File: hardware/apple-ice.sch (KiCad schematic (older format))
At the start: 5 parts

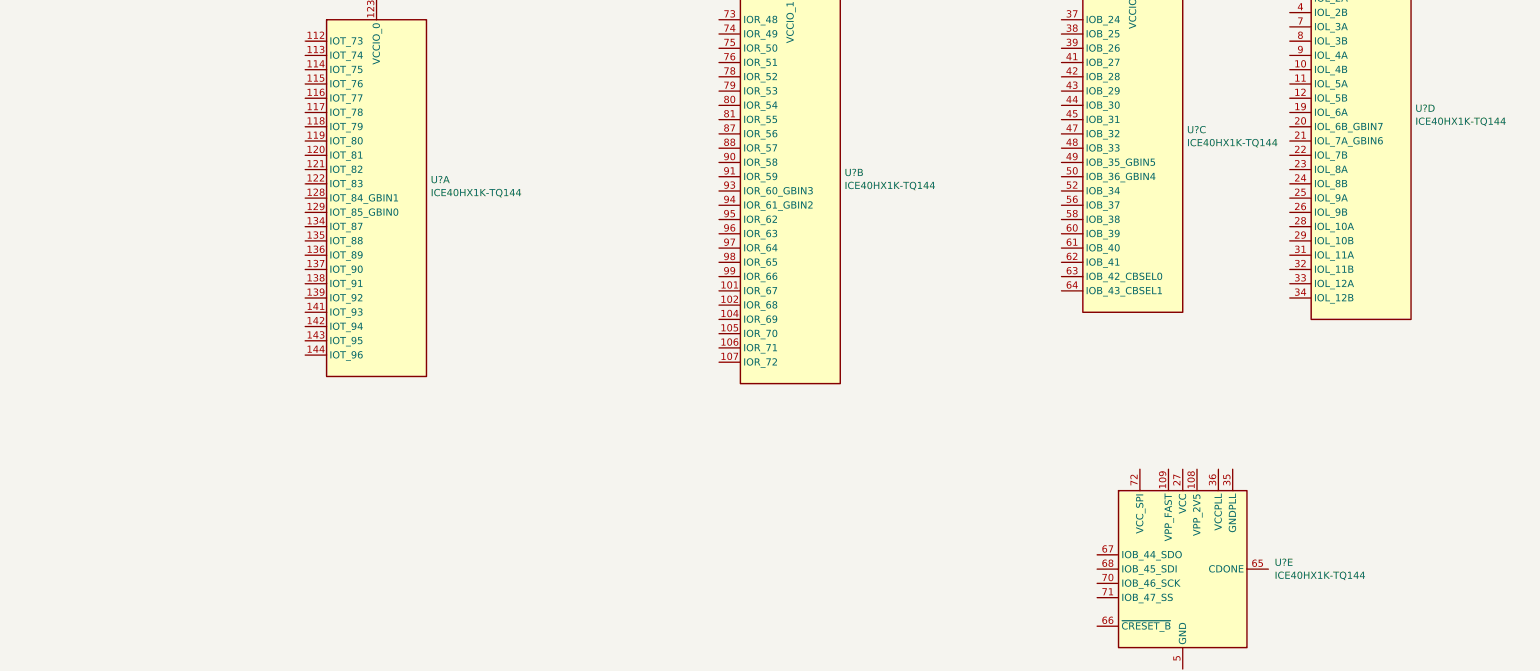
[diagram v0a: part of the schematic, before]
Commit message: Add apple 2 bus/cardedge symbol
Signed-off-by: Rangel Ivanov <rangelivanov88@gmail.com>
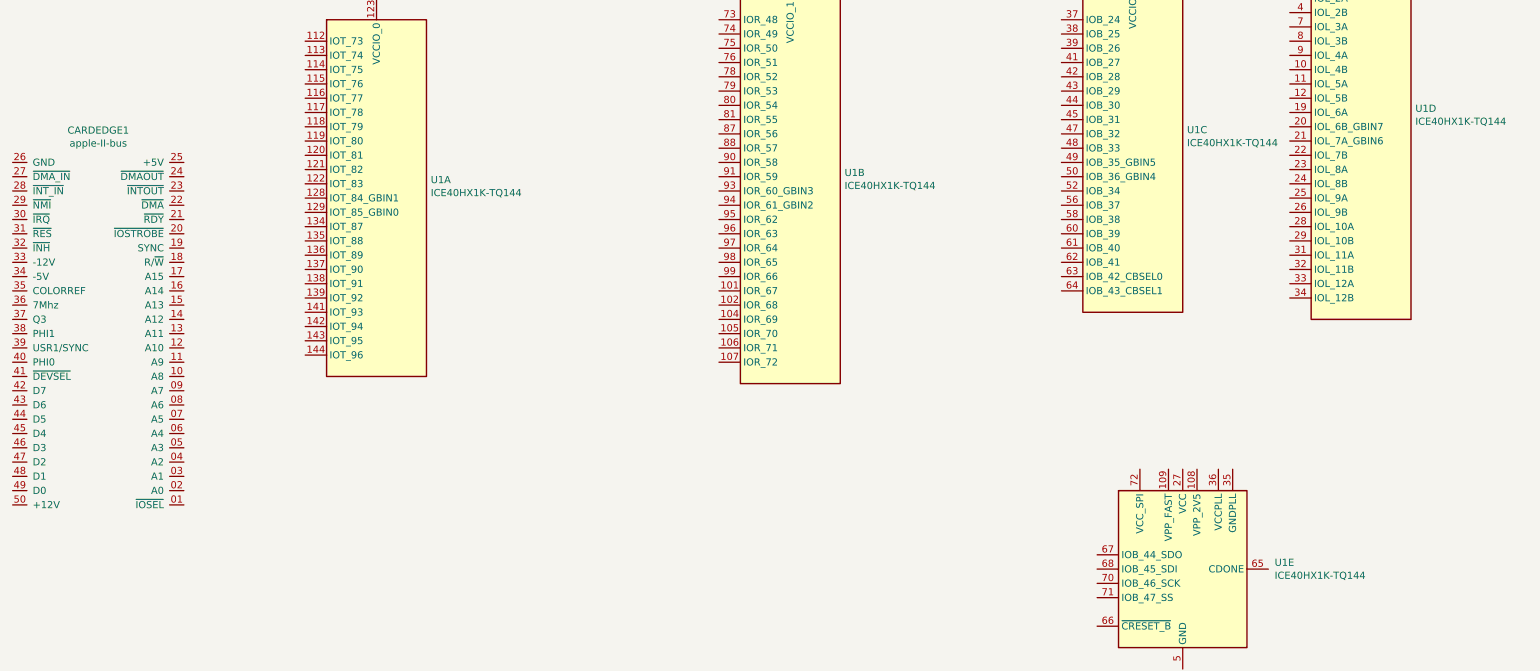
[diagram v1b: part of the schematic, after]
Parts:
- added CARDEDGE1: apple-II-bus, apple-ice:A2-50PIN-MINI, symbol apple-ice:apple-II-bus
- gave numbers to parts that had none: 1
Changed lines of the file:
@@
 $EndDescr
 $Comp
-L apple-ice:ICE40HX1K-TQ144 U?
+L apple-ice:ICE40HX1K-TQ144 U1
 U 1 1 609DDE92
 P 3500 2650
-F 0 "U?" H 3880 2778 50  0000 L CNN
+F 0 "U1" H 3880 2778 50  0000 L CNN
 F 1 "ICE40HX1K-TQ144" H 3880 2687 50  0000 L CNN
 F 2 "apple-ice:TQFP-144_20x20mm_P0.5mm" H 3500 1200 50  0001 C CNN
@@
 $EndComp
 $Comp
-L apple-ice:ICE40HX1K-TQ144 U?
+L apple-ice:ICE40HX1K-TQ144 U1
 U 2 1 609DFA1D
 P 6400 2600
-F 0 "U?" H 6780 2728 50  0000 L CNN
+F 0 "U1" H 6780 2728 50  0000 L CNN
 F 1 "ICE40HX1K-TQ144" H 6780 2637 50  0000 L CNN
 F 2 "apple-ice:TQFP-144_20x20mm_P0.5mm" H 6400 1150 50  0001 C CNN
@@
 $EndComp
 $Comp
-L apple-ice:ICE40HX1K-TQ144 U?
+L apple-ice:ICE40HX1K-TQ144 U1
 U 3 1 609E21D5
 P 8800 2300
-F 0 "U?" H 9180 2428 50  0000 L CNN
+F 0 "U1" H 9180 2428 50  0000 L CNN
 F 1 "ICE40HX1K-TQ144" H 9180 2337 50  0000 L CNN
 F 2 "apple-ice:TQFP-144_20x20mm_P0.5mm" H 8800 850 50  0001 C CNN
@@
 $EndComp
 $Comp
-L apple-ice:ICE40HX1K-TQ144 U?
+L apple-ice:ICE40HX1K-TQ144 U1
 U 4 1 609E4953
 P 10400 2150
-F 0 "U?" H 10780 2278 50  0000 L CNN
+F 0 "U1" H 10780 2278 50  0000 L CNN
 F 1 "ICE40HX1K-TQ144" H 10780 2187 50  0000 L CNN
 F 2 "apple-ice:TQFP-144_20x20mm_P0.5mm" H 10400 700 50  0001 C CNN
@@
 $EndComp
 $Comp
-L apple-ice:ICE40HX1K-TQ144 U?
+L apple-ice:ICE40HX1K-TQ144 U1
 U 5 1 609E76F0
 P 9150 5250
-F 0 "U?" H 9794 5296 50  0000 L CNN
+F 0 "U1" H 9794 5296 50  0000 L CNN
 F 1 "ICE40HX1K-TQ144" H 9794 5205 50  0000 L CNN
 F 2 "apple-ice:TQFP-144_20x20mm_P0.5mm" H 9150 3800 50  0001 C CNN
@@
 	1    0    0    -1
 $EndComp
+$Comp
+L apple-ice:apple-II-bus CARDEDGE1
+U 1 1 60F34519
+P 1550 2250
+F 0 "CARDEDGE1" H 1550 2325 50  0000 C CNN
+F 1 "apple-II-bus" H 1550 2234 50  0000 C CNN
+F 2 "apple-ice:A2-50PIN-MINI" H 1250 2200 50  0001 C CNN
+F 3 "" H 1250 2200 50  0001 C CNN
+	1    1550 2250
+	1    0    0    -1
+$EndComp

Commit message: Symbols and footprints
Signed-off-by: Rangel Ivanov <rangelivanov88@gmail.com>
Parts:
- added J?: USB_B_Micro, symbol apple-ice:USB_B_Micro
- added J?: Conn_02x05_Odd_Even, symbol apple-ice:Conn_02x05_Odd_Even
- added J? (x2): Conn_02x10_Odd_Even, symbol apple-ice:Conn_02x10_Odd_Even
- added U?: W25Q16JVSS, apple-ice:SOIC-8_5.23x5.23mm_P1.27mm, symbol apple-ice:W25Q16JVSS
- added U?: MCP1703A-1202_SOT223, apple-ice:SOT-223-3_TabPin2, symbol apple-ice:MCP1703A-1202_SOT223
- added U?: SN74LVC8T245PW, apple-ice:TSSOP-24_4.4x7.8mm_P0.65mm, symbol apple-ice:SN74LVC8T245PW
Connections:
- new net: U?.11 (GND), U?.12 (GND), U?.13 (GND)
- new net: U?.23 (VCC(B)), U?.24 (VCC(B))
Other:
- moved on the sheet: CARDEDGE1, U1A, U1B, U1C, U1D, U1E
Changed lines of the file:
@@
 L apple-ice:ICE40HX1K-TQ144 U1
 U 1 1 609DDE92
-P 3500 2650
-F 0 "U1" H 3880 2778 50  0000 L CNN
-F 1 "ICE40HX1K-TQ144" H 3880 2687 50  0000 L CNN
-F 2 "apple-ice:TQFP-144_20x20mm_P0.5mm" H 3500 1200 50  0001 C CNN
-F 3 "http://www.latticesemi.com/Products/FPGAandCPLD/iCE40" H 2650 4050 50  0001 C CNN
-	1    3500 2650
+P 3400 2150
+F 0 "U1" H 3780 2278 50  0000 L CNN
+F 1 "ICE40HX1K-TQ144" H 3780 2187 50  0000 L CNN
+F 2 "apple-ice:TQFP-144_20x20mm_P0.5mm" H 3400 700 50  0001 C CNN
+F 3 "http://www.latticesemi.com/Products/FPGAandCPLD/iCE40" H 2550 3550 50  0001 C CNN
+	1    3400 2150
 	1    0    0    -1
 $EndComp
@@
 L apple-ice:ICE40HX1K-TQ144 U1
 U 2 1 609DFA1D
-P 6400 2600
-F 0 "U1" H 6780 2728 50  0000 L CNN
-F 1 "ICE40HX1K-TQ144" H 6780 2637 50  0000 L CNN
-F 2 "apple-ice:TQFP-144_20x20mm_P0.5mm" H 6400 1150 50  0001 C CNN
-F 3 "http://www.latticesemi.com/Products/FPGAandCPLD/iCE40" H 5550 4000 50  0001 C CNN
-	2    6400 2600
+P 5350 2100
+F 0 "U1" H 5730 2228 50  0000 L CNN
+F 1 "ICE40HX1K-TQ144" H 5730 2137 50  0000 L CNN
+F 2 "apple-ice:TQFP-144_20x20mm_P0.5mm" H 5350 650 50  0001 C CNN
+F 3 "http://www.latticesemi.com/Products/FPGAandCPLD/iCE40" H 4500 3500 50  0001 C CNN
+	2    5350 2100
 	1    0    0    -1
 $EndComp
@@
 L apple-ice:ICE40HX1K-TQ144 U1
 U 3 1 609E21D5
-P 8800 2300
-F 0 "U1" H 9180 2428 50  0000 L CNN
-F 1 "ICE40HX1K-TQ144" H 9180 2337 50  0000 L CNN
-F 2 "apple-ice:TQFP-144_20x20mm_P0.5mm" H 8800 850 50  0001 C CNN
-F 3 "http://www.latticesemi.com/Products/FPGAandCPLD/iCE40" H 7950 3700 50  0001 C CNN
-	3    8800 2300
+P 7250 1900
+F 0 "U1" H 7630 2028 50  0000 L CNN
+F 1 "ICE40HX1K-TQ144" H 7630 1937 50  0000 L CNN
+F 2 "apple-ice:TQFP-144_20x20mm_P0.5mm" H 7250 450 50  0001 C CNN
+F 3 "http://www.latticesemi.com/Products/FPGAandCPLD/iCE40" H 6400 3300 50  0001 C CNN
+	3    7250 1900
 	1    0    0    -1
 $EndComp
@@
 L apple-ice:ICE40HX1K-TQ144 U1
 U 4 1 609E4953
-P 10400 2150
-F 0 "U1" H 10780 2278 50  0000 L CNN
-F 1 "ICE40HX1K-TQ144" H 10780 2187 50  0000 L CNN
-F 2 "apple-ice:TQFP-144_20x20mm_P0.5mm" H 10400 700 50  0001 C CNN
-F 3 "http://www.latticesemi.com/Products/FPGAandCPLD/iCE40" H 9550 3550 50  0001 C CNN
-	4    10400 2150
+P 9300 2000
+F 0 "U1" H 9680 2128 50  0000 L CNN
+F 1 "ICE40HX1K-TQ144" H 9680 2037 50  0000 L CNN
+F 2 "apple-ice:TQFP-144_20x20mm_P0.5mm" H 9300 550 50  0001 C CNN
+F 3 "http://www.latticesemi.com/Products/FPGAandCPLD/iCE40" H 8450 3400 50  0001 C CNN
+	4    9300 2000
 	1    0    0    -1
 $EndComp
@@
 L apple-ice:ICE40HX1K-TQ144 U1
 U 5 1 609E76F0
-P 9150 5250
-F 0 "U1" H 9794 5296 50  0000 L CNN
-F 1 "ICE40HX1K-TQ144" H 9794 5205 50  0000 L CNN
-F 2 "apple-ice:TQFP-144_20x20mm_P0.5mm" H 9150 3800 50  0001 C CNN
-F 3 "http://www.latticesemi.com/Products/FPGAandCPLD/iCE40" H 8300 6650 50  0001 C CNN
-	5    9150 5250
+P 8800 4500
+F 0 "U1" H 9444 4546 50  0000 L CNN
+F 1 "ICE40HX1K-TQ144" H 9444 4455 50  0000 L CNN
+F 2 "apple-ice:TQFP-144_20x20mm_P0.5mm" H 8800 3050 50  0001 C CNN
+F 3 "http://www.latticesemi.com/Products/FPGAandCPLD/iCE40" H 7950 5900 50  0001 C CNN
+	5    8800 4500
 	1    0    0    -1
 $EndComp
@@
 L apple-ice:apple-II-bus CARDEDGE1
 U 1 1 60F34519
-P 1550 2250
-F 0 "CARDEDGE1" H 1550 2325 50  0000 C CNN
-F 1 "apple-II-bus" H 1550 2234 50  0000 C CNN
-F 2 "apple-ice:A2-50PIN-MINI" H 1250 2200 50  0001 C CNN
-F 3 "" H 1250 2200 50  0001 C CNN
-	1    1550 2250
+P 1650 800
+F 0 "CARDEDGE1" H 1650 875 50  0000 C CNN
+F 1 "apple-II-bus" H 1650 784 50  0000 C CNN
+F 2 "apple-ice:A2-50PIN-MINI" H 1350 750 50  0001 C CNN
+F 3 "" H 1350 750 50  0001 C CNN
+	1    1650 800
 	1    0    0    -1
 $EndComp
+$Comp
+L apple-ice:W25Q16JVSS U?
+U 1 1 60A599C8
+P 1900 5650
+F 0 "U?" H 1900 6231 50  0000 C CNN
+F 1 "W25Q16JVSS" H 1900 6140 50  0000 C CNN
+F 2 "apple-ice:SOIC-8_5.23x5.23mm_P1.27mm" H 1900 5650 50  0001 C CNN
+F 3 "http://www.winbond.com/resource-files/w25q32jv%20revg%2003272018%20plus.pdf" H 1900 5650 50  0001 C CNN
+	1    1900 5650
+	1    0    0    -1
+$EndComp
+$Comp
+L apple-ice:MCP1703A-1202_SOT223 U?
+U 1 1 60A75D9A
+P 3450 4550
+F 0 "U?" H 3450 4792 50  0000 C CNN
+F 1 "MCP1703A-1202_SOT223" H 3450 4701 50  0000 C CNN
+F 2 "apple-ice:SOT-223-3_TabPin2" H 3450 4750 50  0001 C CNN
+F 3 "http://ww1.microchip.com/downloads/en/DeviceDoc/20005122B.pdf" H 3450 4500 50  0001 C CNN
+	1    3450 4550
+	1    0    0    -1
+$EndComp
+$Comp
+L apple-ice:USB_B_Micro J?
+U 1 1 60A8B864
+P 4900 4750
+F 0 "J?" H 4957 5217 50  0000 C CNN
+F 1 "USB_B_Micro" H 4957 5126 50  0000 C CNN
+F 2 "" H 5050 4700 50  0001 C CNN
+F 3 "~" H 5050 4700 50  0001 C CNN
+	1    4900 4750
+	1    0    0    -1
+$EndComp
+$Comp
+L apple-ice:Conn_02x05_Odd_Even J?
+U 1 1 60B1BC90
+P 6400 4600
+F 0 "J?" H 6450 5017 50  0000 C CNN
+F 1 "Conn_02x05_Odd_Even" H 6450 4926 50  0000 C CNN
+F 2 "" H 6400 4600 50  0001 C CNN
+F 3 "~" H 6400 4600 50  0001 C CNN
+	1    6400 4600
+	1    0    0    -1
+$EndComp
+$Comp
+L apple-ice:Conn_02x10_Odd_Even J?
+U 1 1 60B235DB
+P 9850 5500
+F 0 "J?" H 9900 6117 50  0000 C CNN
+F 1 "Conn_02x10_Odd_Even" H 9900 6026 50  0000 C CNN
+F 2 "" H 9850 5500 50  0001 C CNN
+F 3 "~" H 9850 5500 50  0001 C CNN
+	1    9850 5500
+	1    0    0    -1
+$EndComp
+$Comp
+L apple-ice:Conn_02x10_Odd_Even J?
+U 1 1 60B288E7
+P 7450 4900
+F 0 "J?" H 7500 5517 50  0000 C CNN
+F 1 "Conn_02x10_Odd_Even" H 7500 5426 50  0000 C CNN
+F 2 "" H 7450 4900 50  0001 C CNN
+F 3 "~" H 7450 4900 50  0001 C CNN
+	1    7450 4900
+	1    0    0    -1
+$EndComp
+$Comp
+L apple-ice:SN74LVC8T245PW U?
+U 1 1 60B3B735
+P 4150 6000
+F 0 "U?" H 4150 5111 50  0000 C CNN
+F 1 "SN74LVC8T245PW" H 4150 5020 50  0000 C CNN
+F 2 "apple-ice:TSSOP-24_4.4x7.8mm_P0.65mm" H 4150 4800 50  0001 C CNN
+F 3 "http://www.ti.com/lit/ds/symlink/sn74lvc8t245.pdf" H 4250 6350 50  0001 C CNN
+	1    4150 6000
+	1    0    0    -1
+$EndComp

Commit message: Apple II connections part complete
Edge cuts for board, initial placement of buffers

Signed-off-by: Rangel Ivanov <rangelivanov88@gmail.com>
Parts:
- removed CARDEDGE1: apple-II-bus, apple-ice:A2-50PIN-MINI, symbol apple-ice:apple-II-bus
- removed J?: USB_B_Micro, symbol apple-ice:USB_B_Micro
- removed J?: Conn_02x05_Odd_Even, symbol apple-ice:Conn_02x05_Odd_Even
- removed J? (x2): Conn_02x10_Odd_Even, symbol apple-ice:Conn_02x10_Odd_Even
- added C1, C2, C3, C4: 1uF, symbol apple-ice:C_Small
- added C5, C6, C? (x10): 0.1uF, symbol apple-ice:C_Small
- added J1: TO_SP_DRIVE, apple-ice:IDC-Header_2x10_P2.54mm_Vertical, symbol apple-ice:Conn_02x10_Odd_Even
- added P1: A2Bus-apple2, apple-ice:A2-50PIN-MINI, symbol apple-ice:A2Bus-apple2
- added R1, R2, R4, R5, R6: 22k, symbol apple-ice:R_Small
- added R3: 390, symbol apple-ice:R_Small
- added U10, U2, U4, U5, U9: SN74LVC8T245PW, apple-ice:TSSOP-24_4.4x7.8mm_P0.65mm, symbol apple-ice:SN74LVC8T245PW
- added U6: MCP1703A-3302_SOT223, apple-ice:SOT-223-3_TabPin2, symbol apple-ice:MCP1703A-3302_SOT223
- gave numbers to parts that had none: 3
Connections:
- net ~ENABLE: now reaches U1.73 (IOR_48)
- net ~ENABLE: now also J1.14 (Pin_14)
- net WRDATA: now reaches U1.74 (IOR_49)
- net WRDATA: now also J1.18 (Pin_18)
- net RDDATA_33: now reaches U1.75 (IOR_50)
- net RDDATA_33: now also U2.3 (A1)
- net SENSE_33: now reaches U1.76 (IOR_51)
- net SENSE_33: now also U2.4 (A2)
- net at U1.37 (IOB_24): now also R2.2, U10.22 (~OE)
- net ~RDY: now reaches U1.38 (IOB_25)
- net ~RDY: now also U10.6 (A4)
- net ~INH: now reaches U1.39 (IOB_26)
- net ~INH: now also U10.5 (A3)
- net ~IRQ: now reaches U1.41 (IOB_27)
- net ~IRQ: now also U10.4 (A2)
- net ~NMI: now reaches U1.42 (IOB_28)
- net ~NMI: now also U10.3 (A1)
- net at U1.43 (IOB_29): now also U9.3 (A1)
- net at U1.44 (IOB_30): now also U9.4 (A2)
- net at U1.45 (IOB_31): now also U9.5 (A3)
- net at U1.47 (IOB_32): now also U9.6 (A4)
- net at U1.48 (IOB_33): now also U9.7 (A5)
- net at U1.49 (IOB_35_GBIN5): now also U9.8 (A6)
- net at U1.50 (IOB_36_GBIN4): now also U9.9 (A7)
- net at U1.52 (IOB_34): now also U9.10 (A8)
- net ~D_OE: now reaches U1.56 (IOB_37)
- net ~D_OE: now also U3.22 (~OE), R1.2
- net PH0: now reaches U1.58 (IOB_38)
- net PH0: now also J1.2 (Pin_2)
- net PH1: now reaches U1.60 (IOB_39)
- net PH1: now also J1.4 (Pin_4)
- net PH2: now reaches U1.61 (IOB_40)
- net PH2: now also J1.6 (Pin_6)
- net PH3: now reaches U1.62 (IOB_41)
- net PH3: now also J1.8 (Pin_8)
- net ~WREQ: now reaches U1.63 (IOB_42_CBSEL0)
- net ~WREQ: now also J1.10 (Pin_10)
- net SEL: now reaches U1.64 (IOB_43_CBSEL1)
- net SEL: now also J1.12 (Pin_12)
- net D0_33: now reaches U1.1 (IOL_1A)
- net D0_33: now also U3.10 (A8)
- net D7_33: now reaches U1.10 (IOL_4B)
- net D7_33: now also U3.3 (A1)
- net A0_33: now reaches U1.11 (IOL_5A)
- net A0_33: now also U4.10 (A8)
- net A1_33: now reaches U1.12 (IOL_5B)
- net A1_33: now also U4.9 (A7)
- net A2_33: now reaches U1.19 (IOL_6A)
- net A2_33: now also U4.8 (A6)
- net D1_33: now reaches U1.2 (IOL_1B)
- net D1_33: now also U3.9 (A7)
- net A3_33: now reaches U1.20 (IOL_6B_GBIN7)
- net A3_33: now also U4.7 (A5)
- net A4_33: now reaches U1.21 (IOL_7A_GBIN6)
- net A4_33: now also U4.6 (A4)
- net A5_33: now reaches U1.22 (IOL_7B)
- net A5_33: now also U4.5 (A3)
- net A6_33: now reaches U1.23 (IOL_8A)
- net A6_33: now also U4.4 (A2)
- net A7_33: now reaches U1.24 (IOL_8B)
- net A7_33: now also U4.3 (A1)
- net A8_33: now reaches U1.25 (IOL_9A)
- net A8_33: now also U5.10 (A8)
- net A9_33: now reaches U1.26 (IOL_9B)
- net A9_33: now also U5.9 (A7)
- net A10_33: now reaches U1.28 (IOL_10A)
- net A10_33: now also U5.8 (A6)
- net A11_33: now reaches U1.29 (IOL_10B)
- net A11_33: now also U5.7 (A5)
- net D2_33: now reaches U1.3 (IOL_2A)
- net D2_33: now also U3.8 (A6)
- net A12_33: now reaches U1.31 (IOL_11A)
- net A12_33: now also U5.6 (A4)
- net A13_33: now reaches U1.32 (IOL_11B)
- net A13_33: now also U5.5 (A3)
- net A14_33: now reaches U1.33 (IOL_12A)
- net A14_33: now also U5.4 (A2)
- net A15_33: now reaches U1.34 (IOL_12B)
- net A15_33: now also U5.3 (A1)
- net D3_33: now reaches U1.4 (IOL_2B)
- net D3_33: now also U3.7 (A5)
- net D4_33: now reaches U1.7 (IOL_3A)
- net D4_33: now also U3.6 (A4)
- net D5_33: now reaches U1.8 (IOL_3B)
- net D5_33: now also U3.5 (A3)
- net D6_33: now reaches U1.9 (IOL_4A)
- net D6_33: now also U3.4 (A2)
- net +5V: now reaches U7.1 (VI)
- net +5V: now also U3.23 (VCC(B)), U3.24 (VCC(B)), C1.1, C2.1, C5.2, C?.2, C?.2, C?.2, C?.2, C?.2, J1.11 (Pin_11), P1.25 (+5V), R5.1, R6.1, U10.1 (VCC(A)), U2.23 (VCC(B)), U2.24 (VCC(B)), U4.23 (VCC(B)), U4.24 (VCC(B)), U5.23 (VCC(B)), U5.24 (VCC(B)), U6.1 (VI), U9.23 (VCC(B)), U9.24 (VCC(B))
- net GND: now reaches U7.2 (GND)
- net GND: now also U3.11 (GND), U3.12 (GND), U3.13 (GND), C1.2, C2.2, C3.2, C4.2, C5.1, C6.1, C?.1, C?.1, C?.1, C?.1, C?.1, C?.1, C?.1, C?.1, C?.1, C?.1, J1.1 (Pin_1), J1.3 (Pin_3), U10.11 (GND), U10.12 (GND), U10.13 (GND), U10.14 (B8), U10.15 (B7), U10.16 (B6), U10.17 (B5), U2.11 (GND), U2.12 (GND), U2.13 (GND), U2.14 (B8), U2.15 (B7), U2.16 (B6), U2.17 (B5), U2.18 (B4), U2.19 (B3), U2.2 (DIR), U2.22 (~OE), U4.11 (GND), U4.12 (GND), U4.13 (GND), U4.2 (DIR), U4.22 (~OE), U5.11 (GND), U5.12 (GND), U5.13 (GND), U5.2 (DIR), U5.22 (~OE), U6.2 (GND), U9.11 (GND), U9.12 (GND), U9.13 (GND), U9.2 (DIR), U9.22 (~OE)
- net 1.2V: now reaches U7.3 (VO)
- net 1.2V: now also C4.1
- net 3.3V: now reaches U3.1 (VCC(A))
- net 3.3V: now also C3.1, C6.2, C?.2, C?.2, C?.2, C?.2, C?.2, R1.1, R2.1, R4.1, U10.23 (VCC(B)), U10.24 (VCC(B)), U2.1 (VCC(A)), U4.1 (VCC(A)), U5.1 (VCC(A)), U6.3 (VO), U9.1 (VCC(A))
- net D0: now reaches U3.14 (B8)
- net D0: now also P1.49 (D0)
- net D1: now reaches U3.15 (B7)
- net D1: now also P1.48 (D1)
- net D2: now reaches U3.16 (B6)
- net D2: now also P1.47 (D2)
- net D3: now reaches U3.17 (B5)
- net D3: now also P1.46 (D3)
- net D4: now reaches U3.18 (B4)
- net D4: now also P1.45 (D4)
- net D5: now reaches U3.19 (B3)
- net D5: now also P1.44 (D5)
- net RW: now reaches U3.2 (DIR)
- net RW: now also P1.18 (R/~W), U9.21 (B1)
- net D6: now reaches U3.20 (B2)
- net D6: now also P1.43 (D6)
- net D7: now reaches U3.21 (B1)
- net D7: now also P1.42 (D7)
- new net: R4.2, U10.2 (DIR)
- new net: P1.21 (~RDY), U10.18 (B4)
- new net: P1.32 (~INH), U10.19 (B3)
- new net: P1.30 (~IRQ), U10.20 (B2)
- new net: P1.29 (~NMI), U10.21 (B1)
- new net: P1.36 (7M), U9.14 (B8)
- new net: R3.1, U9.15 (B7)
- new net: P1.40 (PHI0), U9.16 (B6)
- new net: P1.31 (~RES), U9.17 (B5)
- new net: P1.41 (~DEVSEL), U9.18 (B4)
- new net: P1.20 (~IOSTRB), U9.19 (B3)
- new net: P1.01 (~IOSEL), U9.20 (B2)
- new net: P1.23 (~INTOUT), P1.28 (~INTIN)
- new net: P1.24 (~DMAOUT), P1.27 (~DMAIN)
- new net: P1.37 (Q3), R3.2
- new net -12V: J1.9 (Pin_9)
- new net 12V: J1.13 (Pin_13), J1.15 (Pin_15)
- new net A0: P1.02 (A0), U4.14 (B8)
- new net A1: P1.03 (A1), U4.15 (B7)
- new net A10: P1.12 (A10), U5.16 (B6)
- new net A11: P1.13 (A11), U5.17 (B5)
- new net A12: P1.14 (A12), U5.18 (B4)
- new net A13: P1.15 (A13), U5.19 (B3)
- new net A14: P1.16 (A14), U5.20 (B2)
- new net A15: P1.17 (A15), U5.21 (B1)
- new net A2: P1.04 (A2), U4.16 (B6)
- new net A3: P1.05 (A3), U4.17 (B5)
- new net A4: P1.06 (A4), U4.18 (B4)
- new net A5: P1.07 (A5), U4.19 (B3)
- new net A6: P1.08 (A6), U4.20 (B2)
- new net A7: P1.09 (A7), U4.21 (B1)
- new net A8: P1.10 (A8), U5.14 (B8)
- new net A9: P1.11 (A9), U5.15 (B7)
- new net RDDATA: J1.16 (Pin_16), R6.2, U2.21 (B1)
- new net SENSE: J1.20 (Pin_20), R5.2, U2.20 (B2)
- new net ~ENABLE2: J1.5 (Pin_5)
- no-connect marks 0 -> 19
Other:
- moved on the sheet: U1A, U1B, U1C, U1D, U1E, U3, U7, U8
